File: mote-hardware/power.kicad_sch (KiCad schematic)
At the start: 11 parts, among them J1 USB_C_Receptacle_USB2.0_14P, U2 NCP1117-3.3_SOT223

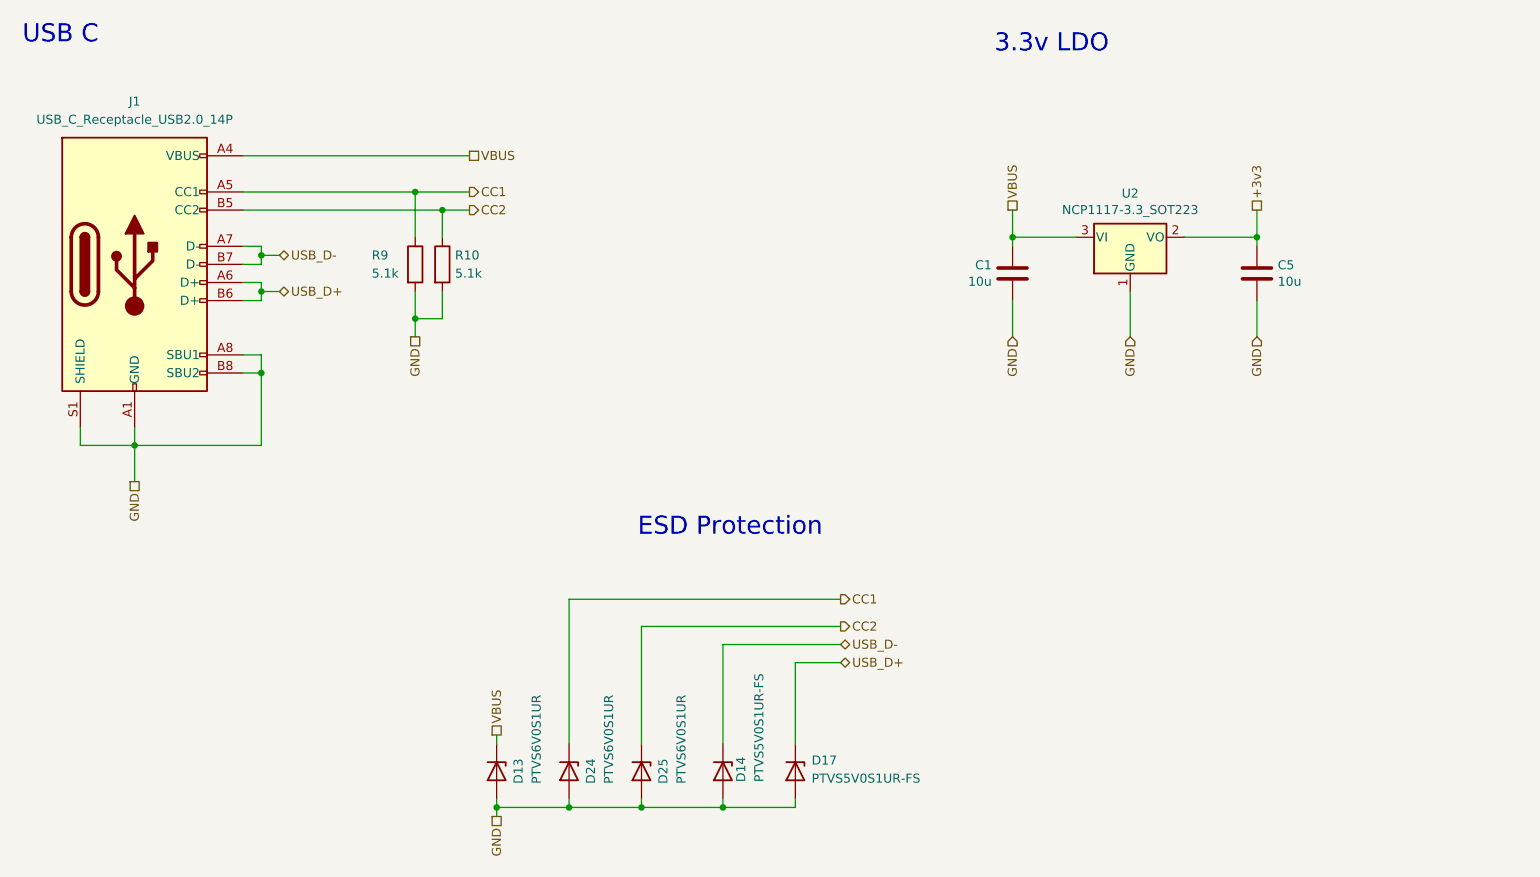
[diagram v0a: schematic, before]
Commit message: Update schematic with low cap / high speed TVS diodes
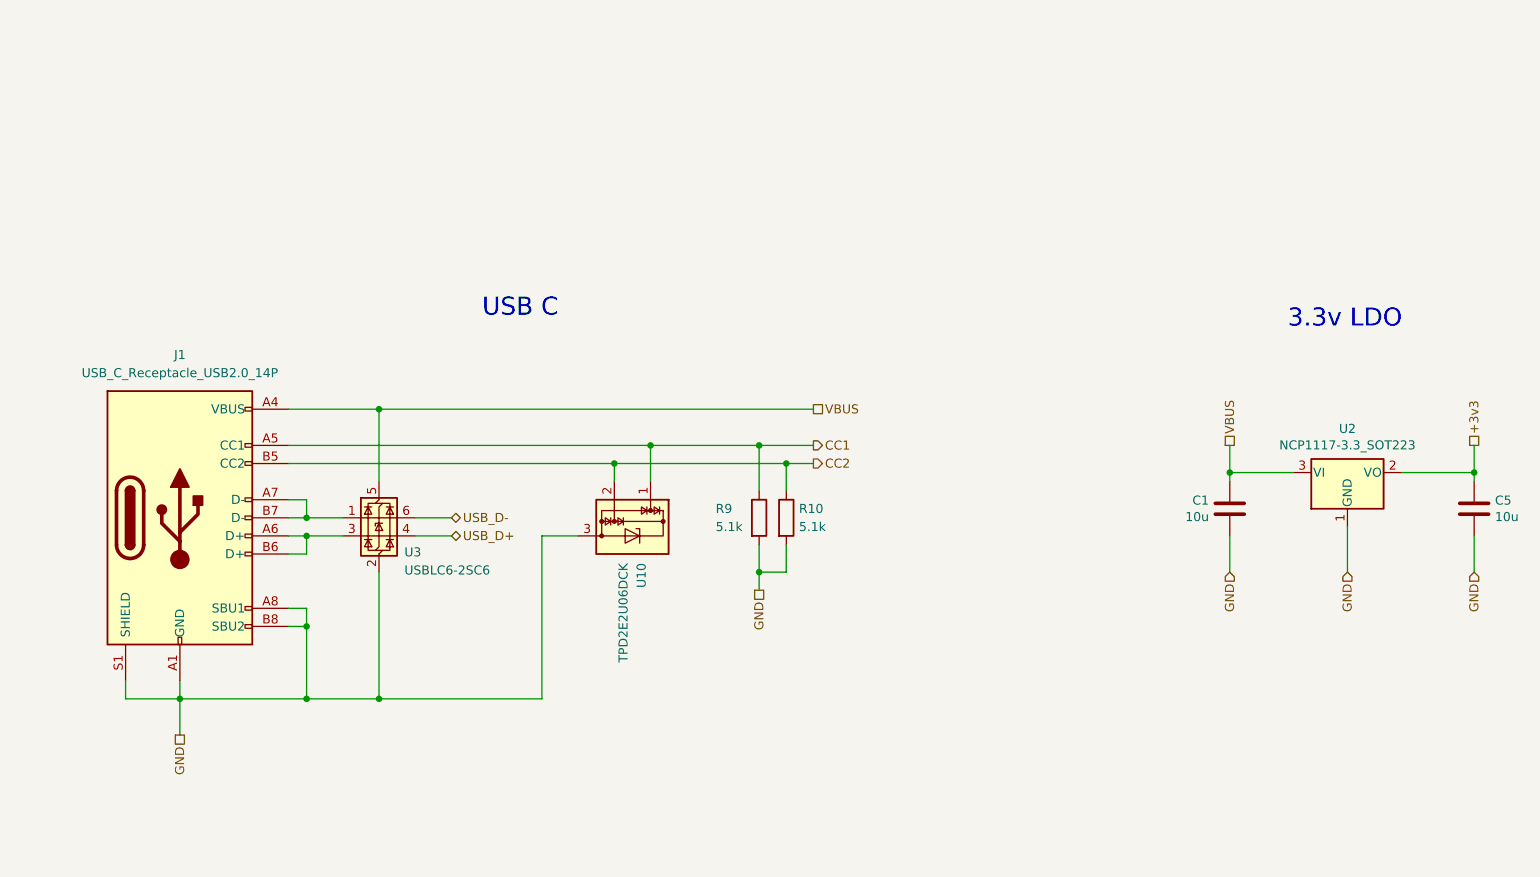
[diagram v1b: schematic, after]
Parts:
- removed D13, D24, D25: PTVS6V0S1UR, Diode_SMD:D_SOD-123, symbol Diode:PTVS7V5Z1USK
- removed D14, D17: PTVS5V0S1UR-FS, Diode_SMD:D_SOD-123, symbol Diode:PTVS5V0Z1USK
- added U10: TPD2E2U06DCK, Package_TO_SOT_SMD:SOT-323_SC-70, symbol Power_Protection:TPD2E2U06DCK
- added U3: USBLC6-2SC6, Package_TO_SOT_SMD:SOT-23-6, symbol Power_Protection:USBLC6-2SC6
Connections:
- net CC1: now also U10.1
- net CC2: now also U10.2
- net GND: now also U10.3, U3.2 (GND)
- net USB_D+: now also U3.4 (I/O2); no longer J1.A6 (D+), J1.B6 (D+)
- net USB_D-: now also U3.6 (I/O1); no longer J1.A7 (D-), J1.B7 (D-)
- net VBUS: now also U3.5 (VBUS)
- new net: J1.A6 (D+), J1.B6 (D+), U3.3 (I/O2)
- new net: J1.A7 (D-), J1.B7 (D-), U3.1 (I/O1)
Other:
- note removed: "ESD Protection"
- moved on the sheet: C1, C5, J1, R10, R9, U2

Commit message: Layout for new tvs diodes
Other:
- company: github.com/empriselab/mote-core -> github.com/empriselab/mote
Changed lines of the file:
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@@
 	(title_block
 		(title "Mote")
-		(date "2026-04-25")
-		(rev "V0.1.0")
-		(company "github.com/empriselab/mote-core")
+		(date "2026-05-25")
+		(rev "V0.2.0")
+		(company "github.com/empriselab/mote")
 	)
 	(text "USB C"
